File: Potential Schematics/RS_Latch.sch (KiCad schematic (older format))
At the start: 2 parts

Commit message: Made the registers
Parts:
- gave numbers to parts that had none: 1
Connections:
- net Q: now also U1.10, U1.11; no longer U1.1, U1.2
- net QN: now also U1.13, U1.9; no longer U1.1, U1.3
- net R: now also U1.8; no longer U1.2
- net S: now also U1.12; no longer U1.3

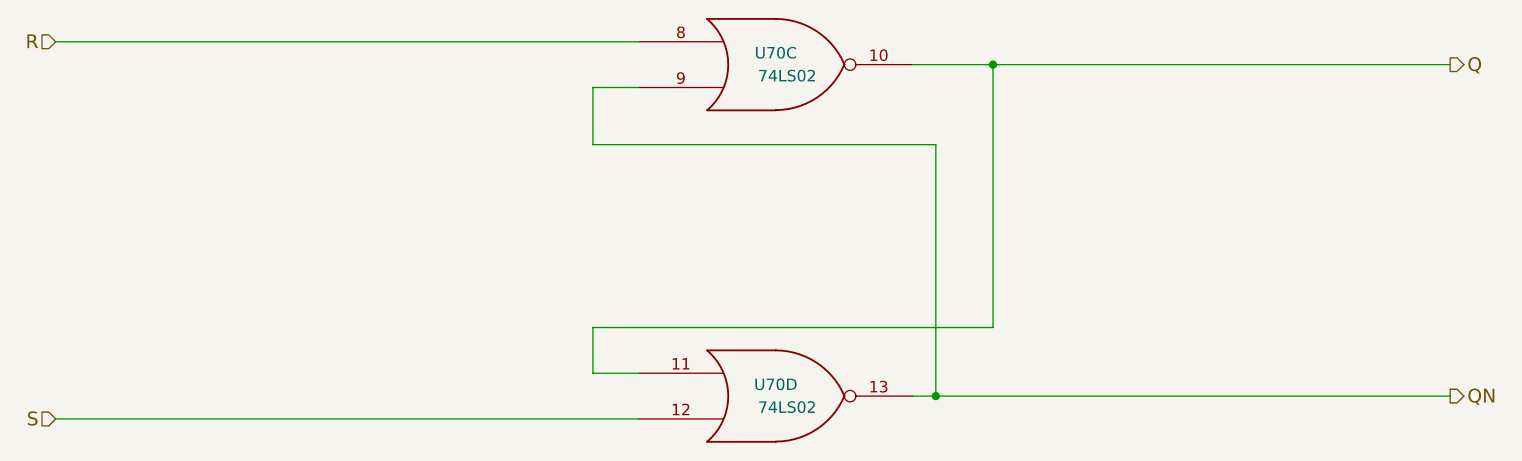
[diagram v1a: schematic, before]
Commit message: Added Registers to Top Schematic
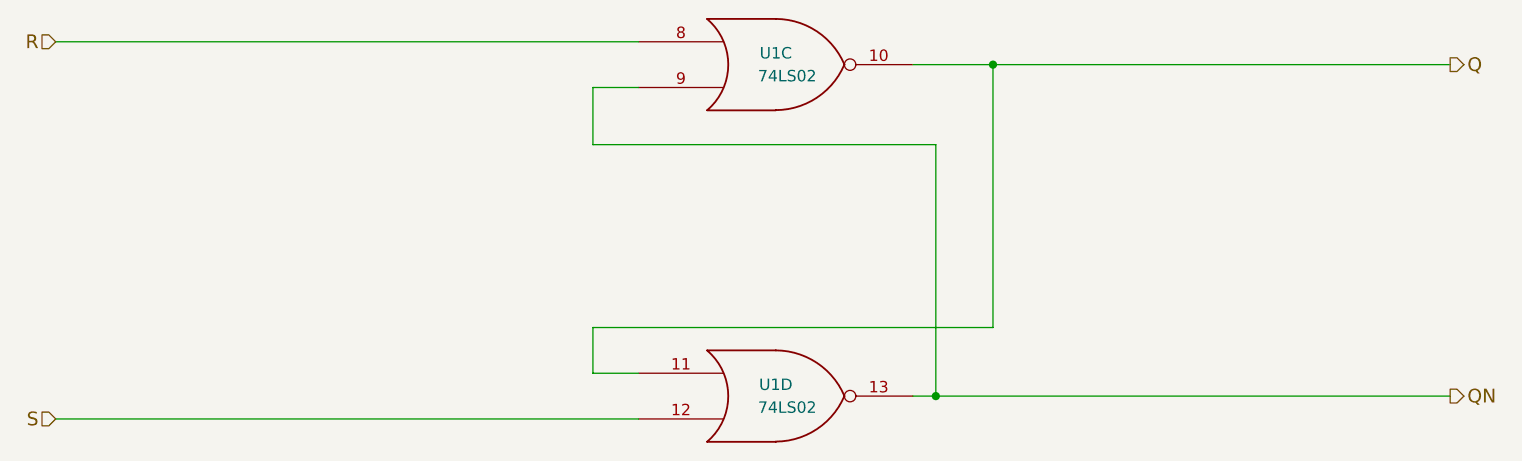
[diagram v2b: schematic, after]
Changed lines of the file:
@@
 $Descr A4 11693 8268
 encoding utf-8
-Sheet 132 449
+Sheet 27 449
 Title "RS Latch"
 Date "2018-09-14"
@@
 AR Path="/5B9D167A/5B9C0EA0/5B9DB28B/5B9C41DB/5B9C0F1C/5B9C12D5/5B9D7015" Ref="U178"  Part="3"
 AR Path="/5B9D167A/5B9C0EA0/5B9DB28B/5B9C41DB/5B9C312A/5B9C12D5/5B9D7015" Ref="U180"  Part="1"
-F 0 "U70" H 5950 3050 50  0000 C CNN
+F 0 "U1" H 5950 3050 50  0000 C CNN
 F 1 "74LS02" H 6000 2950 50  0000 C CNN
 F 2 "" H 5950 3000 50  0001 C CNN
@@
 AR Path="/5B9D167A/5B9C0EA0/5B9DB28B/5B9C41DB/5B9C0F1C/5B9C12D5/5B9D70E7" Ref="U178"  Part="4"
 AR Path="/5B9D167A/5B9C0EA0/5B9DB28B/5B9C41DB/5B9C312A/5B9C12D5/5B9D70E7" Ref="U180"  Part="2"
-F 0 "U70" H 5950 4500 50  0000 C CNN
+F 0 "U1" H 5950 4500 50  0000 C CNN
 F 1 "74LS02" H 6000 4400 50  0000 C CNN
 F 2 "" H 5950 4450 50  0001 C CNN

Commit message: Adding Multiply Devide
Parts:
- U1: symbol 74LS02 -> 4-bit_processor-rescue:74LS02
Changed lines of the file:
@@
-EESchema Schematic File Version 2
-LIBS:power
-LIBS:device
-LIBS:switches
-LIBS:relays
-LIBS:motors
-LIBS:transistors
-LIBS:conn
-LIBS:linear
-LIBS:regul
-LIBS:74xx
-LIBS:cmos4000
-LIBS:adc-dac
-LIBS:memory
-LIBS:xilinx
-LIBS:microcontrollers
-LIBS:dsp
-LIBS:microchip
-LIBS:analog_switches
-LIBS:motorola
-LIBS:texas
-LIBS:intel
-LIBS:audio
-LIBS:interface
-LIBS:digital-audio
-LIBS:philips
-LIBS:display
-LIBS:cypress
-LIBS:siliconi
-LIBS:opto
-LIBS:atmel
-LIBS:contrib
-LIBS:valves
+EESchema Schematic File Version 4
 LIBS:4-bit_processor-cache
-EELAYER 25 0
+EELAYER 26 0
 EELAYER END
 $Descr A4 11693 8268
 encoding utf-8
-Sheet 27 449
+Sheet 27 451
 Title "RS Latch"
 Date "2018-09-14"
@@
 QN
 $Comp
-L 74LS02 U1
+L 4-bit_processor-rescue:74LS02 U1
 U 3 1 5B9D7015
 P 5950 3000
@@
 AR Path="/5B9D167A/5B9C0EA0/5B9DB28B/5B9C41DB/5B9C0F1C/5B9C12D5/5B9D7015" Ref="U178"  Part="3"
 AR Path="/5B9D167A/5B9C0EA0/5B9DB28B/5B9C41DB/5B9C312A/5B9C12D5/5B9D7015" Ref="U180"  Part="1"
+AR Path="/5B9D7015" Ref="U1"  Part="3"
 F 0 "U1" H 5950 3050 50  0000 C CNN
 F 1 "74LS02" H 6000 2950 50  0000 C CNN
@@
 $EndComp
 $Comp
-L 74LS02 U1
+L 4-bit_processor-rescue:74LS02 U1
 U 4 1 5B9D70E7
 P 5950 4450
@@
 AR Path="/5B9D167A/5B9C0EA0/5B9DB28B/5B9C41DB/5B9C0F1C/5B9C12D5/5B9D70E7" Ref="U178"  Part="4"
 AR Path="/5B9D167A/5B9C0EA0/5B9DB28B/5B9C41DB/5B9C312A/5B9C12D5/5B9D70E7" Ref="U180"  Part="2"
+AR Path="/5B9D70E7" Ref="U1"  Part="4"
 F 0 "U1" H 5950 4500 50  0000 C CNN
 F 1 "74LS02" H 6000 4400 50  0000 C CNN

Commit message: Finished PCB
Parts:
- U29: renamed from U1; footprint (none) -> Daniel_Kopp:DIP-14_300_ELL
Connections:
- net Q: now also U29.1, U29.5; no longer U29.10, U29.11
- net QN: now also U29.3, U29.4; no longer U29.13, U29.9
- net R: now also U29.2; no longer U29.8
- net S: now also U29.6; no longer U29.12
